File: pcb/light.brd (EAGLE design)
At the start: 13 x 13 mm, 4 parts, among them J3 FFC3B07-05-T, U1 TEMT6000

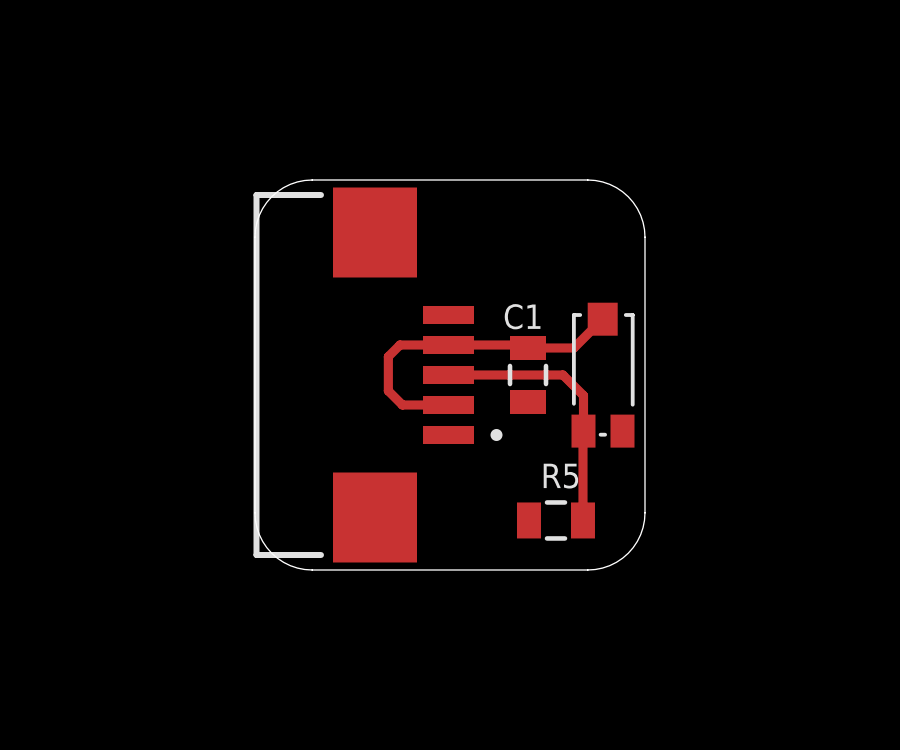
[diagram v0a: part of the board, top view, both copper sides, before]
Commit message: added website
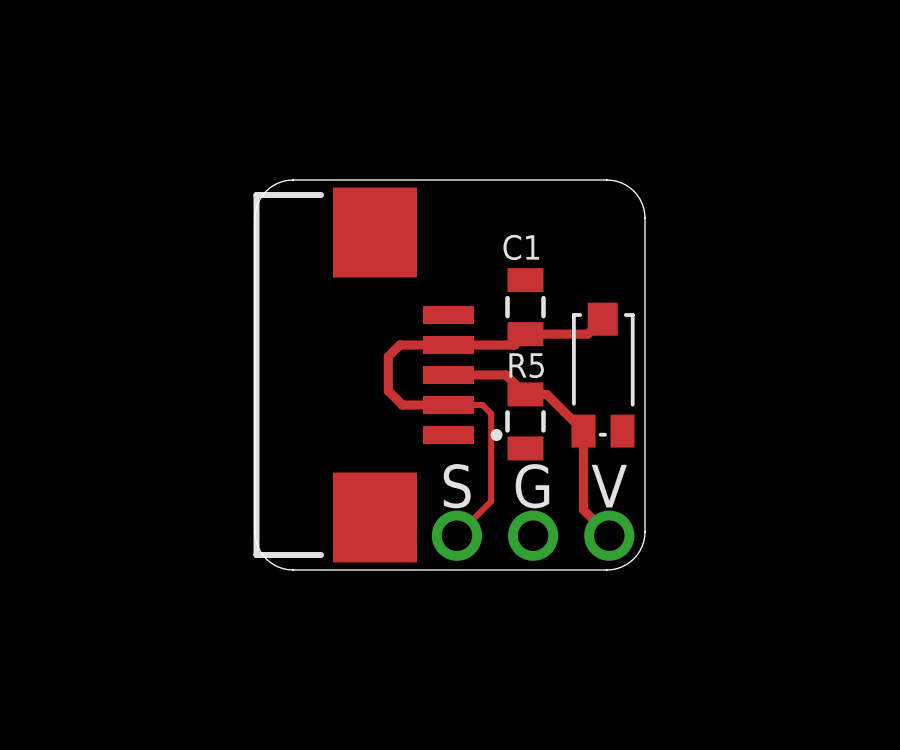
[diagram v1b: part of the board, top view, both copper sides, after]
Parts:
- added JP1: (no value), adafruit_changed:1X03-CLEANBIG
- moved R5 3.45 mm to (9.02, 4.95), turned to 90 degrees
- moved C1 2.26 mm to (9.02, 8.76), turned to 270 degrees
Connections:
- net +3V3: now also JP1.1
- net GND: now also JP1.2
- net S: now also JP1.3
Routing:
- net +3V3: track 11.1 -> 17.1 mm
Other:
- outline, holes or cut-outs redrawn
- board text added: "G"
- board text added: "PulseHPT.com dekuNukem 2023"
- board text added: "S"
- board text added: "V"
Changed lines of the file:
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@@
 <board>
 <plain>
-<wire x1="11.095" y1="0" x2="1.905" y2="0" width="0" layer="20"/>
-<wire x1="1.905" y1="0" x2="0" y2="1.905" width="0" layer="20" curve="-90"/>
-<wire x1="0" y1="1.905" x2="0" y2="11.095" width="0" layer="20"/>
-<wire x1="0" y1="11.095" x2="1.905" y2="13" width="0" layer="20" curve="-90"/>
-<wire x1="1.905" y1="13" x2="11.095" y2="13" width="0" layer="20"/>
-<wire x1="11.095" y1="13" x2="13" y2="11.095" width="0" layer="20" curve="-90"/>
-<wire x1="13" y1="11.095" x2="13" y2="1.905" width="0" layer="20"/>
-<wire x1="13" y1="1.905" x2="11.095" y2="0" width="0" layer="20" curve="-90"/>
+<wire x1="11.73" y1="0" x2="1.27" y2="0" width="0" layer="20"/>
+<wire x1="1.27" y1="0" x2="0" y2="1.27" width="0" layer="20" curve="-90"/>
+<wire x1="0" y1="1.27" x2="0" y2="11.73" width="0" layer="20"/>
+<wire x1="0" y1="11.73" x2="1.27" y2="13" width="0" layer="20" curve="-90"/>
+<wire x1="1.27" y1="13" x2="11.73" y2="13" width="0" layer="20"/>
+<wire x1="11.73" y1="13" x2="13" y2="11.73" width="0" layer="20" curve="-90"/>
+<wire x1="13" y1="11.73" x2="13" y2="1.27" width="0" layer="20"/>
+<wire x1="13" y1="1.27" x2="11.73" y2="0" width="0" layer="20" curve="-90"/>
+<text x="6.731" y="2.794" size="1.4224" layer="25" rot="R180" align="center">S</text>
+<text x="9.271" y="2.794" size="1.4224" layer="25" rot="R180" align="center">G</text>
+<text x="11.811" y="2.794" size="1.4224" layer="25" rot="R180" align="center">V</text>
+<text x="6.604" y="6.731" size="1.27" layer="26" rot="MR0" align="center">PulseHPT.com
+dekuNukem
+2023</text>
 </plain>
 <attributes>
@@
 </element>
 <element name="U1" library="SparkFun" package="TEMT6000-SEN" value="TEMT6000" x="11.6" y="6.5" smashed="yes" rot="R90"/>
-<element name="R5" library="joyAnalog" package="0805" value="10K" x="10.033" y="1.651" smashed="yes">
-<attribute name="NAME" x="9.525" y="2.7305" size="0.8128" layer="25"/>
+<element name="R5" library="joyAnalog" package="0805" value="10K" x="9.017" y="4.953" smashed="yes" rot="R90">
+<attribute name="NAME" x="8.382" y="6.4135" size="0.8128" layer="25"/>
 </element>
-<element name="C1" library="clock" package="0805" value="100nF" x="9.1" y="6.5" smashed="yes" rot="R90">
-<attribute name="NAME" x="9.608" y="8.8495" size="0.8128" layer="25" rot="R180"/>
+<element name="C1" library="clock" package="0805" value="100nF" x="9.017" y="8.763" smashed="yes" rot="R270">
+<attribute name="NAME" x="9.564" y="11.1585" size="0.8128" layer="25" rot="R180"/>
+</element>
+<element name="JP1" library="adafruit_changed" package="1X03-CLEANBIG" value="" x="9.271" y="1.143" smashed="yes">
+<attribute name="VALUE" x="5.461" y="-2.032" size="1.27" layer="27"/>
 </element>
 </elements>
@@
 <contactref element="R5" pad="1"/>
 <contactref element="C1" pad="1"/>
+<contactref element="JP1" pad="2"/>
 </signal>
 <signal name="S">
@@
 <contactref element="J3" pad="3"/>
 <contactref element="R5" pad="2"/>
-<wire x1="10.95" y1="4.63" x2="10.95" y2="5.814" width="0.3048" layer="1"/>
-<wire x1="10.264" y1="6.5" x2="6.45" y2="6.5" width="0.3048" layer="1"/>
-<wire x1="10.95" y1="5.814" x2="10.264" y2="6.5" width="0.3048" layer="1"/>
-<wire x1="10.933" y1="1.651" x2="10.933" y2="4.613" width="0.3048" layer="1"/>
-<wire x1="10.933" y1="4.613" x2="10.95" y2="4.63" width="0.3048" layer="1"/>
+<wire x1="6.45" y1="6.5" x2="8.37" y2="6.5" width="0.3048" layer="1"/>
+<wire x1="8.37" y1="6.5" x2="9.017" y2="5.853" width="0.3048" layer="1"/>
+<wire x1="9.017" y1="5.853" x2="9.727" y2="5.853" width="0.3048" layer="1"/>
+<wire x1="9.727" y1="5.853" x2="10.95" y2="4.63" width="0.3048" layer="1"/>
+<contactref element="JP1" pad="3"/>
+<wire x1="10.95" y1="4.63" x2="10.95" y2="2.004" width="0.3048" layer="1"/>
+<wire x1="10.95" y1="2.004" x2="11.811" y2="1.143" width="0.3048" layer="1"/>
 </signal>
 <signal name="+3V3">
@@
 <wire x1="4.914" y1="5.5" x2="6.45" y2="5.5" width="0.3048" layer="1"/>
 <wire x1="4.445" y1="5.969" x2="4.914" y2="5.5" width="0.3048" layer="1"/>
-<wire x1="6.45" y1="7.5" x2="9" y2="7.5" width="0.3048" layer="1"/>
-<wire x1="9" y1="7.5" x2="9.1" y2="7.4" width="0.3048" layer="1"/>
-<wire x1="9.1" y1="7.4" x2="10.63" y2="7.4" width="0.3048" layer="1"/>
-<wire x1="10.63" y1="7.4" x2="11.59" y2="8.36" width="0.3048" layer="1"/>
+<wire x1="6.45" y1="7.5" x2="8.654" y2="7.5" width="0.3048" layer="1"/>
+<wire x1="8.654" y1="7.5" x2="9.017" y2="7.863" width="0.3048" layer="1"/>
+<wire x1="9.017" y1="7.863" x2="11.093" y2="7.863" width="0.3048" layer="1"/>
+<wire x1="11.093" y1="7.863" x2="11.59" y2="8.36" width="0.3048" layer="1"/>
+<contactref element="JP1" pad="1"/>
+<wire x1="6.45" y1="5.5" x2="7.581" y2="5.5" width="0.2032" layer="1"/>
+<wire x1="7.874" y1="2.286" x2="6.731" y2="1.143" width="0.2032" layer="1"/>
+<wire x1="7.581" y1="5.5" x2="7.874" y2="5.207" width="0.2032" layer="1"/>
+<wire x1="7.874" y1="5.207" x2="7.874" y2="2.286" width="0.2032" layer="1"/>
 </signal>
 </signals>
@@
 </board>
 </drawing>
+<compatibility>
+<note version="6.3" minversion="6.2.2" severity="warning">
+Since Version 6.2.2 text objects can contain more than one line,
+which will not be processed correctly with this version.
+</note>
+</compatibility>
 </eagle>
